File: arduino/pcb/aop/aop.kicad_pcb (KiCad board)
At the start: 2 copper layers, 45 x 55 mm, 22 parts, among them Q1 AO4435, SW1 SW_Push, SW2 SW_Push, U1 ESP32-C3_SUPERMINI_TH, U2 DS3231M

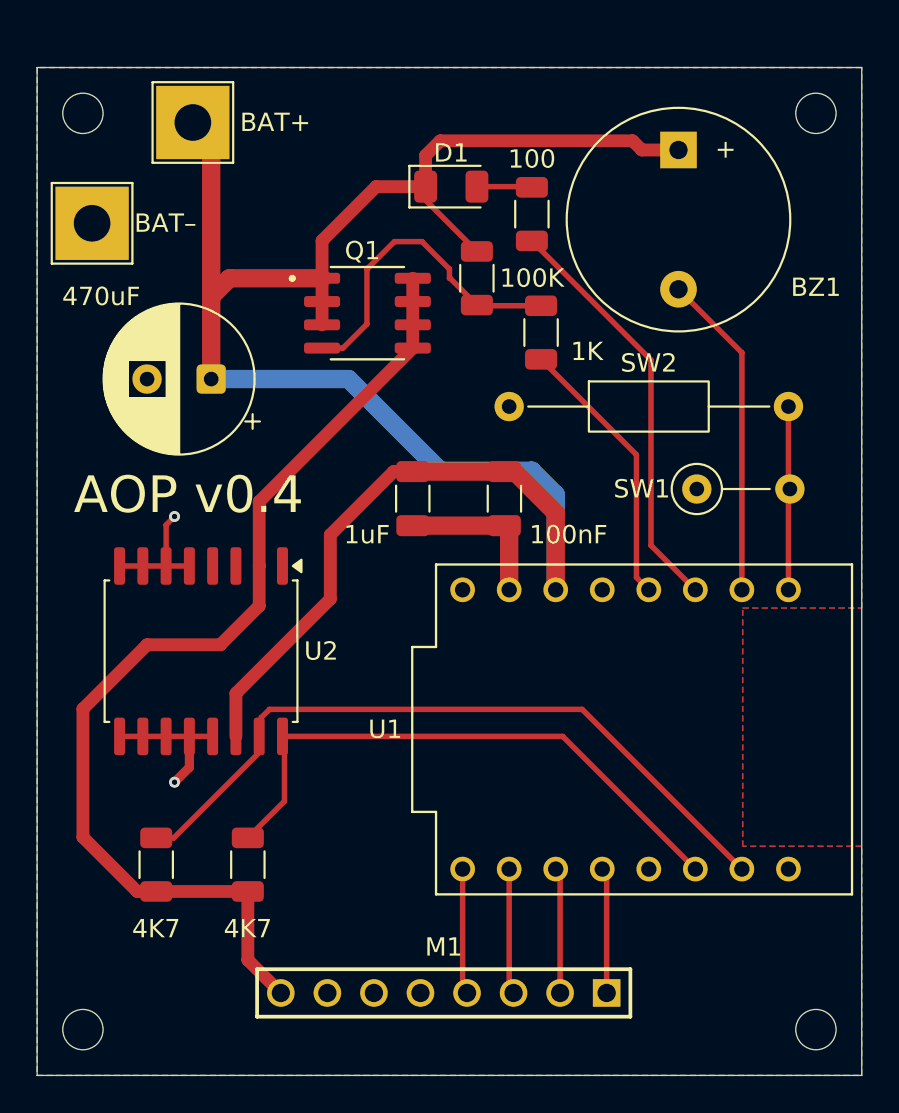
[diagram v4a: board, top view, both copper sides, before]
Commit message: [pcb] Move SDA to GPIO4 to avoid clash with UART
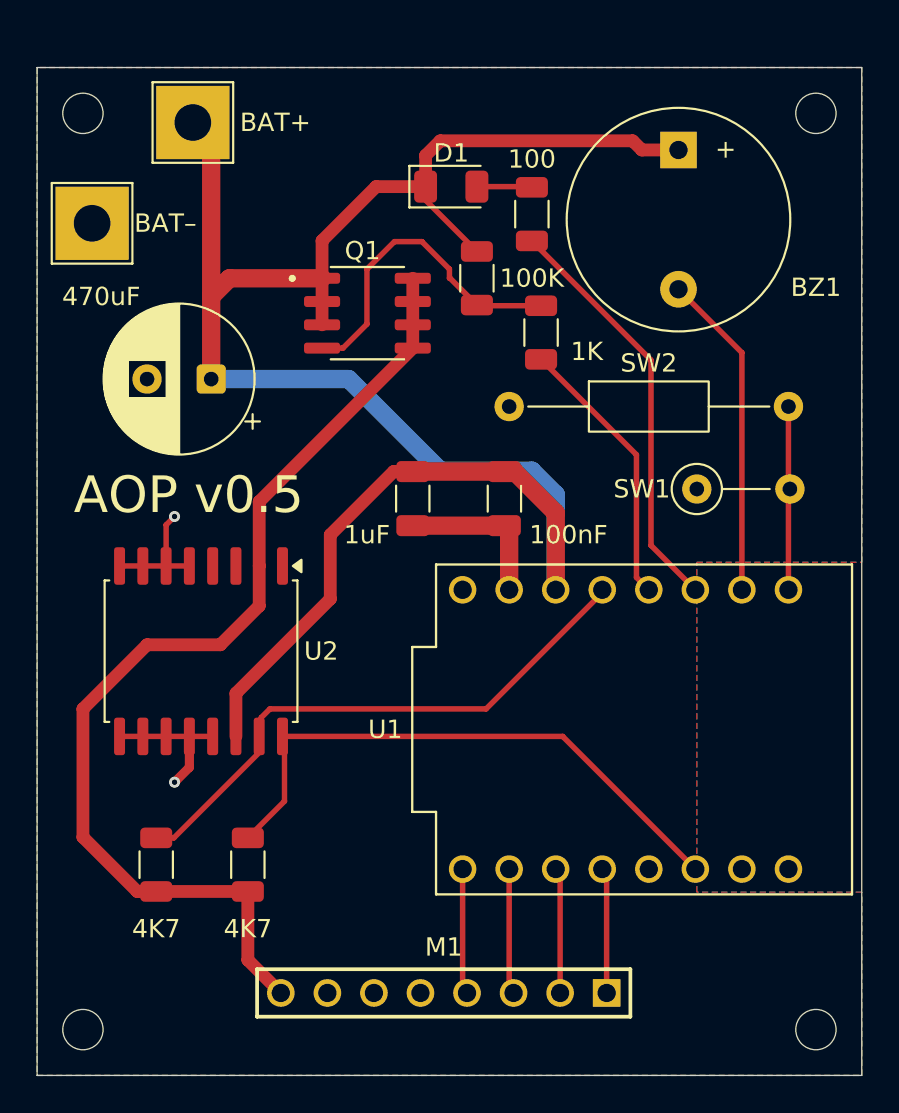
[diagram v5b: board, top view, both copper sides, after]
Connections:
- R4 pad 2: Net-(U1-GPIO20) -> Net-(U1-GPIO4)
- U1 pad 20: Net-(U1-GPIO20) -> unconnected-(U1-GPIO20-Pad20)
- U1 pad 4: unconnected-(U1-GPIO4-Pad4) -> Net-(U1-GPIO4)
- U2 pad 15: Net-(U1-GPIO20) -> Net-(U1-GPIO4)
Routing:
- net Net-(U1-GPIO20): track 39.5 -> 0.00 mm
- net Net-(U1-GPIO4): track 0.00 -> 31.1 mm
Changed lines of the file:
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@@
 	(title_block
 		(title "AOP")
-		(rev "v0.4")
+		(rev "v0.5")
 	)
 	(layers
@@
 			(layers "F.Cu" "F.Mask" "F.Paste")
 			(roundrect_rratio 0.222222)
-			(net "Net-(U1-GPIO20)")
+			(net "Net-(U1-GPIO4)")
 			(pintype "passive")
 		)
@@
 			(layers "F.Cu" "F.Mask" "F.Paste")
 			(roundrect_rratio 0.25)
-			(net "Net-(U1-GPIO20)")
+			(net "Net-(U1-GPIO4)")
 			(pinfunction "SDA_15")
 			(pintype "bidirectional")
@@
 		(sheetname "/")
 		(sheetfile "aop.kicad_sch")
-		(units
-			(unit
-				(name "A")
-				(pins "0" "1" "2" "3" "4" "5" "6" "5V" "3.3" "7" "8" "9" "10" "20" "21"
-					"G"
-				)
-			)
-		)
 		(attr through_hole dnp)
 		(duplicate_pad_numbers_are_jumpers no)
@@
 		(pad "0" thru_hole circle
 			(at 7.62 7.88 90)
-			(size 1.348 1.348)
-			(drill 0.84)
+			(size 1.5 1.5)
+			(drill 1)
 			(layers "*.Cu" "*.Mask")
 			(remove_unused_layers no)
@@
 		(pad "1" thru_hole circle
 			(at 7.62 5.34 90)
-			(size 1.348 1.348)
-			(drill 0.84)
+			(size 1.5 1.5)
+			(drill 1)
 			(layers "*.Cu" "*.Mask")
 			(remove_unused_layers no)
@@
 		(pad "2" thru_hole circle
 			(at 7.62 2.8 90)
-			(size 1.348 1.348)
-			(drill 0.84)
+			(size 1.5 1.5)
+			(drill 1)
 			(layers "*.Cu" "*.Mask")
 			(remove_unused_layers no)
@@
 		(pad "3" thru_hole circle
 			(at 7.62 0.26 90)
-			(size 1.348 1.348)
-			(drill 0.84)
+			(size 1.5 1.5)
+			(drill 1)
 			(layers "*.Cu" "*.Mask")
 			(remove_unused_layers no)
@@
 		(pad "3.3" thru_hole circle
 			(at 7.62 -4.82 90)
-			(size 1.348 1.348)
-			(drill 0.84)
+			(size 1.5 1.5)
+			(drill 1)
 			(layers "*.Cu" "*.Mask")
 			(remove_unused_layers no)
@@
 		(pad "4" thru_hole circle
 			(at 7.62 -2.28 90)
-			(size 1.348 1.348)
-			(drill 0.84)
+			(size 1.5 1.5)
+			(drill 1)
 			(layers "*.Cu" "*.Mask")
 			(remove_unused_layers no)
-			(net "unconnected-(U1-GPIO4-Pad4)")
+			(net "Net-(U1-GPIO4)")
 			(pinfunction "GPIO4_4")
 			(pintype "bidirectional")
@@
 		(pad "5" thru_hole circle
 			(at -7.62 -9.9 90)
-			(size 1.348 1.348)
-			(drill 0.84)
+			(size 1.5 1.5)
+			(drill 1)
 			(layers "*.Cu" "*.Mask")
 			(remove_unused_layers no)
@@
 		(pad "5V" thru_hole circle
 			(at 7.62 -9.9 90)
-			(size 1.348 1.348)
-			(drill 0.84)
+			(size 1.5 1.5)
+			(drill 1)
 			(layers "*.Cu" "*.Mask")
 			(remove_unused_layers no)
@@
 		(pad "6" thru_hole circle
 			(at -7.62 -7.36 90)
-			(size 1.348 1.348)
-			(drill 0.84)
+			(size 1.5 1.5)
+			(drill 1)
 			(layers "*.Cu" "*.Mask")
 			(remove_unused_layers no)
@@
 		(pad "7" thru_hole circle
 			(at -7.62 -4.82 90)
-			(size 1.348 1.348)
-			(drill 0.84)
+			(size 1.5 1.5)
+			(drill 1)
 			(layers "*.Cu" "*.Mask")
 			(remove_unused_layers no)
@@
 		(pad "8" thru_hole circle
 			(at -7.62 -2.28 90)
-			(size 1.348 1.348)
-			(drill 0.84)
+			(size 1.5 1.5)
+			(drill 1)
 			(layers "*.Cu" "*.Mask")
 			(remove_unused_layers no)
@@
 		(pad "9" thru_hole circle
 			(at -7.62 0.26 90)
-			(size 1.348 1.348)
-			(drill 0.84)
+			(size 1.5 1.5)
+			(drill 1)
 			(layers "*.Cu" "*.Mask")
 			(remove_unused_layers no)
@@
 		(pad "10" thru_hole circle
 			(at -7.62 2.8 90)
-			(size 1.348 1.348)
-			(drill 0.84)
+			(size 1.5 1.5)
+			(drill 1)
 			(layers "*.Cu" "*.Mask")
 			(remove_unused_layers no)
@@
 		(pad "20" thru_hole circle
 			(at -7.62 5.34 90)
-			(size 1.348 1.348)
-			(drill 0.84)
+			(size 1.5 1.5)
+			(drill 1)
 			(layers "*.Cu" "*.Mask")
 			(remove_unused_layers no)
-			(net "Net-(U1-GPIO20)")
+			(net "unconnected-(U1-GPIO20-Pad20)")
 			(pinfunction "GPIO20_20")
 			(pintype "bidirectional")
@@
 		(pad "21" thru_hole circle
 			(at -7.62 7.88 90)
-			(size 1.348 1.348)
-			(drill 0.84)
+			(size 1.5 1.5)
+			(drill 1)
 			(layers "*.Cu" "*.Mask")
 			(remove_unused_layers no)
@@
 		(pad "G" thru_hole circle
 			(at 7.62 -7.36 90)
-			(size 1.348 1.348)
-			(drill 0.84)
+			(size 1.5 1.5)
+			(drill 1)
 			(layers "*.Cu" "*.Mask")
 			(remove_unused_layers no)
@@
 	)
 	(segment
-		(start 138.680001 115.525)
-		(end 138.23 115.975001)
+		(start 159.5 106.58)
+		(end 159.5 96.4625)
 		(width 0.3)
 		(layer "F.Cu")
-		(net "Net-(U1-GPIO20)")
+		(net "Net-(U1-GPIO2)")
 	)
 	(segment
-		(start 138.23 117.77)
-		(end 133.4625 122.5375)
+		(start 161.92 109)
+		(end 159.5 106.58)
 		(width 0.3)
 		(layer "F.Cu")
-		(net "Net-(U1-GPIO20)")
+		(net "Net-(U1-GPIO2)")
 	)
 	(segment
-		(start 155.745 115.525)
-		(end 138.680001 115.525)
+		(start 159.5 96.4625)
+		(end 153 89.9625)
 		(width 0.3)
 		(layer "F.Cu")
-		(net "Net-(U1-GPIO20)")
+		(net "Net-(U1-GPIO2)")
 	)
 	(segment
-		(start 138.23 117)
-		(end 138.23 117.77)
+		(start 152.5 87)
+		(end 150 87)
 		(width 0.3)
 		(layer "F.Cu")
-		(net "Net-(U1-GPIO20)")
+		(net "Net-(D1-A)")
 	)
 	(segment
-		(start 138.23 115.975001)
-		(end 138.23 117)
+		(start 161.92 124.24)
+		(end 154.68 117)
 		(width 0.3)
 		(layer "F.Cu")
-		(net "Net-(U1-GPIO20)")
+		(net "Net-(U1-GPIO10)")
 	)
 	(segment
-		(start 164.46 124.24)
-		(end 155.745 115.525)
+		(start 139.5 117)
+		(end 139.5 120.5375)
 		(width 0.3)
 		(layer "F.Cu")
-		(net "Net-(U1-GPIO20)")
+		(net "Net-(U1-GPIO10)")
 	)
 	(segment
-		(start 133.4625 122.5375)
-		(end 132.5 122.5375)
+		(start 154.68 117)
+		(end 139.5 117)
 		(width 0.3)
 		(layer "F.Cu")
-		(net "Net-(U1-GPIO20)")
+		(net "Net-(U1-GPIO10)")
 	)
 	(segment
-		(start 159.5 106.58)
-		(end 159.5 96.4625)
+		(start 139.5 120.5375)
+		(end 137.5 122.5375)
 		(width 0.3)
 		(layer "F.Cu")
-		(net "Net-(U1-GPIO2)")
+		(net "Net-(U1-GPIO10)")
 	)
 	(segment
-		(start 161.92 109)
-		(end 159.5 106.58)
+		(start 156.84 109.16)
+		(end 156.84 109)
 		(width 0.3)
 		(layer "F.Cu")
-		(net "Net-(U1-GPIO2)")
+		(net "Net-(U1-GPIO4)")
 	)
 	(segment
-		(start 159.5 96.4625)
-		(end 153 89.9625)
+		(start 133.4625 122.5375)
+		(end 138.23 117.77)
 		(width 0.3)
 		(layer "F.Cu")
-		(net "Net-(U1-GPIO2)")
+		(net "Net-(U1-GPIO4)")
 	)
 	(segment
-		(start 152.5 87)
-		(end 150 87)
+		(start 150.5 115.5)
+		(end 156.84 109.16)
 		(width 0.3)
 		(layer "F.Cu")
-		(net "Net-(D1-A)")
+		(net "Net-(U1-GPIO4)")
 	)
 	(segment
-		(start 161.92 124.24)
-		(end 154.68 117)
+		(start 138.23 117.77)
+		(end 138.23 115.975001)
 		(width 0.3)
 		(layer "F.Cu")
-		(net "Net-(U1-GPIO10)")
+		(net "Net-(U1-GPIO4)")
 	)
 	(segment
-		(start 139.5 117)
-		(end 139.5 120.5375)
+		(start 132.5 122.5375)
+		(end 133.4625 122.5375)
 		(width 0.3)
 		(layer "F.Cu")
-		(net "Net-(U1-GPIO10)")
+		(net "Net-(U1-GPIO4)")
 	)
 	(segment
-		(start 154.68 117)
-		(end 139.5 117)
+		(start 138.705001 115.5)
+		(end 150.5 115.5)
 		(width 0.3)
 		(layer "F.Cu")
-		(net "Net-(U1-GPIO10)")
+		(net "Net-(U1-GPIO4)")
 	)
 	(segment
-		(start 139.5 120.5375)
-		(end 137.5 122.5375)
+		(start 138.23 115.975001)
+		(end 138.705001 115.5)
 		(width 0.3)
 		(layer "F.Cu")
-		(net "Net-(U1-GPIO10)")
+		(net "Net-(U1-GPIO4)")
 	)
 	(zone
@@
 		(min_thickness 0.25)
 		(fill yes
-			(mode hatch)
 			(thermal_gap 0.5)
 			(thermal_bridge_width 0.5)
-			(smoothing fillet)
 			(island_removal_mode 0)
-			(hatch_thickness 10)
-			(hatch_gap 2)
-			(hatch_orientation 0)
-			(hatch_smoothing_level 2)
-			(hatch_smoothing_value 0.2)
-			(hatch_border_algorithm hatch_thickness)
-			(hatch_min_hole_area 0.15)
 		)
 		(polygon
 			(pts
-				(xy 126 80.5) (xy 126 135.5) (xy 171 135.5) (xy 171 123) (xy 164.5 123) (xy 164.5 110) (xy 171 110)
+				(xy 126 80.5) (xy 126 135.5) (xy 171 135.5) (xy 171 125.5) (xy 162 125.5) (xy 162 107.5) (xy 171 107.5)
 				(xy 171 80.5)
 			)

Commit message: [pcb] Use GPIO20 for SPI_SS because GPIO8 is high in the deep sleep
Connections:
- U1 pad 20: unconnected-(U1-GPIO20-Pad20) -> Net-(M1-SDA)
- U1 pad 8: Net-(M1-SDA) -> unconnected-(U1-GPIO8-Pad8)
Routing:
- net Net-(M1-SDA): track 6.86 -> 11.2 mm
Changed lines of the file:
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@@
 		(sheetname "/")
 		(sheetfile "aop.kicad_sch")
+		(units
+			(unit
+				(name "A")
+				(pins "0" "1" "2" "3" "4" "5" "6" "5V" "3.3" "7" "8" "9" "10" "20" "21"
+					"G"
+				)
+			)
+		)
 		(attr through_hole dnp)
 		(duplicate_pad_numbers_are_jumpers no)
@@
 			(layers "*.Cu" "*.Mask")
 			(remove_unused_layers no)
-			(net "Net-(M1-SDA)")
+			(net "unconnected-(U1-GPIO8-Pad8)")
 			(pinfunction "GPIO8_8")
 			(pintype "bidirectional")
@@
 			(layers "*.Cu" "*.Mask")
 			(remove_unused_layers no)
-			(net "unconnected-(U1-GPIO20-Pad20)")
+			(net "Net-(M1-SDA)")
 			(pinfunction "GPIO20_20")
 			(pintype "bidirectional")
@@
 	)
 	(segment
+		(start 159.58 128.5)
+		(end 161.96 128.5)
+		(width 0.3)
+		(layer "F.Cu")
+		(net "Net-(M1-SDA)")
+	)
+	(segment
 		(start 157.08 131)
-		(end 157.08 124.48)
+		(end 159.58 128.5)
 		(width 0.3)
 		(layer "F.Cu")
@@
 	)
 	(segment
-		(start 157.08 124.48)
-		(end 156.84 124.24)
+		(start 161.96 128.5)
+		(end 164.46 126)
+		(width 0.3)
+		(layer "F.Cu")
+		(net "Net-(M1-SDA)")
+	)
+	(segment
+		(start 164.46 126)
+		(end 164.46 124.24)
 		(width 0.3)
 		(layer "F.Cu")
@@
 		(net "Net-(U1-GPIO4)")
 	)
+	(segment
+		(start 157.08 124.48)
+		(end 156.84 124.24)
+		(width 0.3)
+		(layer "F.Cu")
+		(net "unconnected-(U1-GPIO8-Pad8)")
+	)
 	(zone
